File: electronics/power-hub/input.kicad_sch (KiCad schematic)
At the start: 12 parts, among them J1 24V IN, Q1 SUD50P06-15

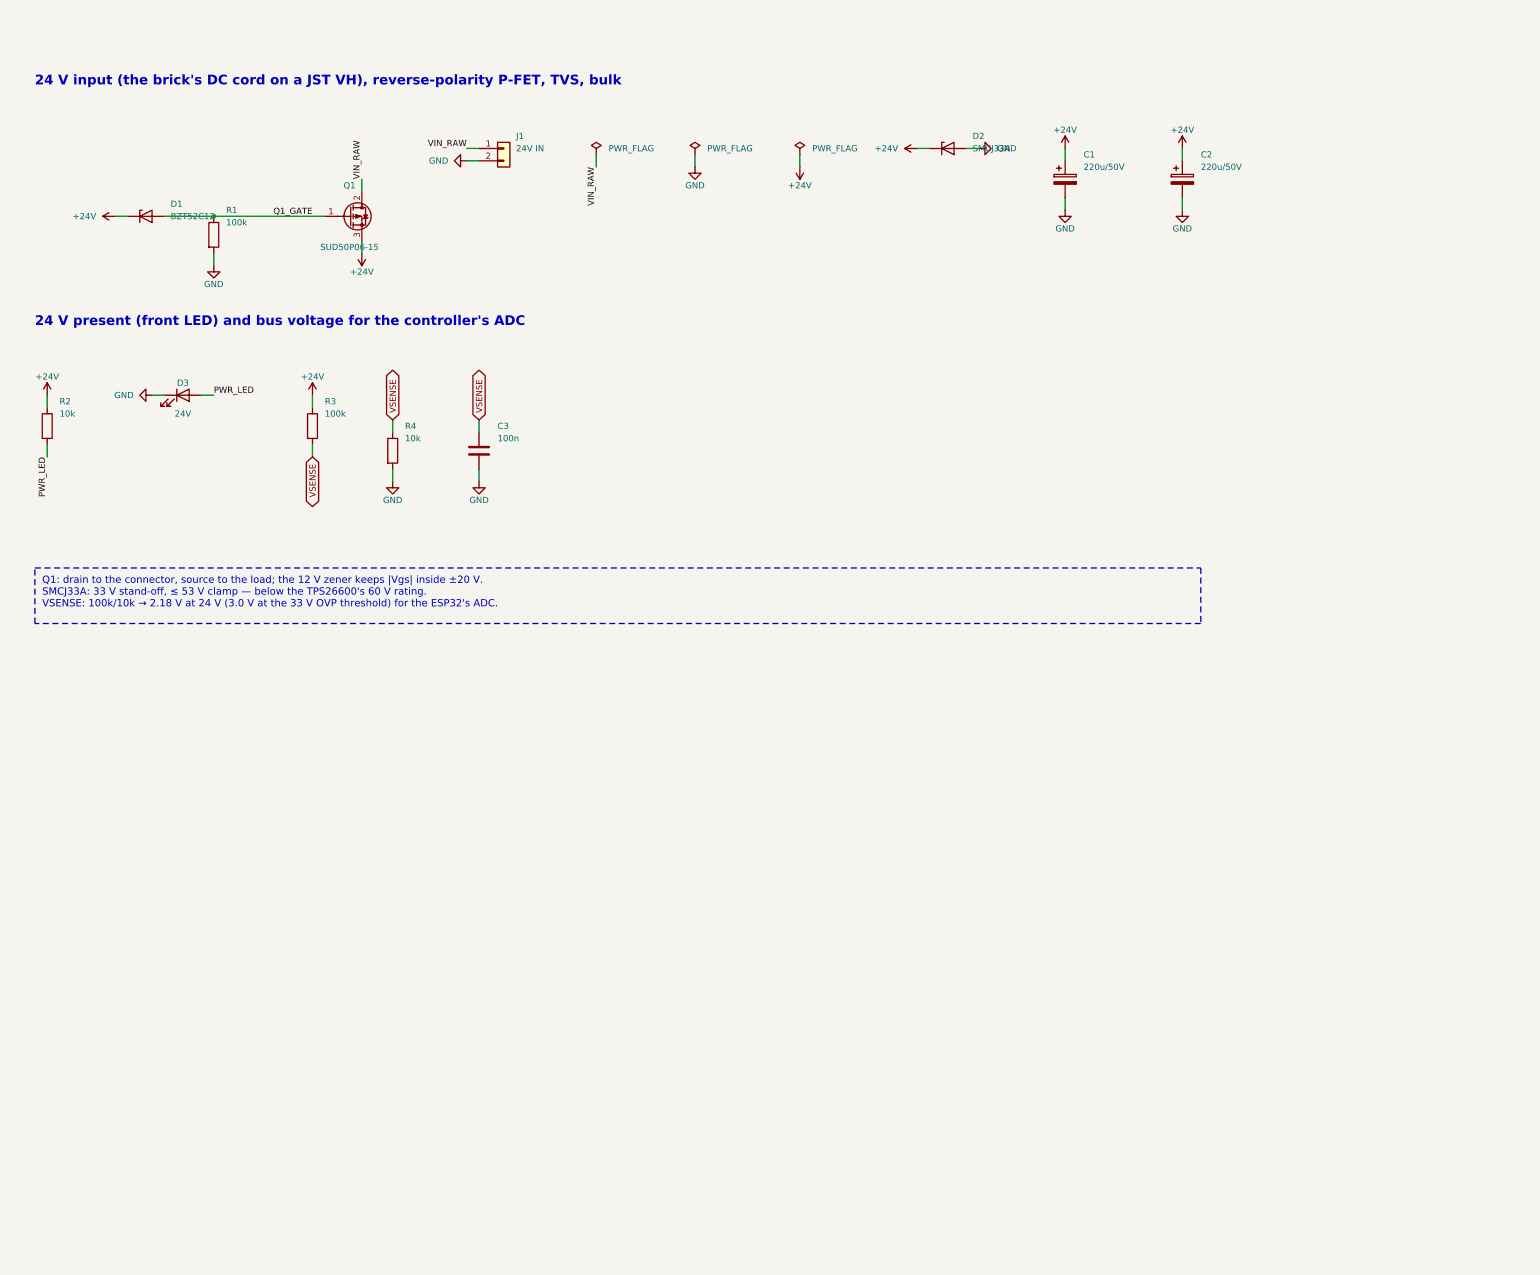
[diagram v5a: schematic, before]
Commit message: Power hub v0.5: USB-C PD input (AP33772S), 4 layers, rows off until enabled
The rack now runs from one USB PD 3.1 charger instead of the GST60A24 brick.

Hub v0.5 (76 x 140 mm, 4 layers, In1 GND, In2 VRACK/+3V3):
* AP33772S sink: 20 V at power-up (VSEL 39k), 28 V EPR on the controller's
  request, never 36/48 V; 5 mOhm Kelvin shunt, back-to-back IRF7842 switch,
  SMAJ30A TVS, NTC by the switch, interrupt and I2C to the ESP32-S3.
* USB4105 5 A receptacle; the controller's buck runs from VBUS (5-28 V),
  ahead of the switch.
* Every row's TPS26600 is off until the controller drives ROW_EN (SHDN pulled
  low); IMON per row; front PD LED.
* ERC 0, DRC 0 errors, 0 unconnected, parity 0; 146 3D models, 0 stand-ins.

Power box: 84 x 148 x 35 mm, hub only (no brick, no cradles), rear USB-C
cut-out, lid on corner lugs.  Viewer, BOM (charger + 5 A e-marked cable,
4-layer JLC estimate) and docs (power, mechanical, cabling, assembly,
electronics) follow.

Co-Authored-By: Claude Opus 5.5 <noreply@anthropic.com>
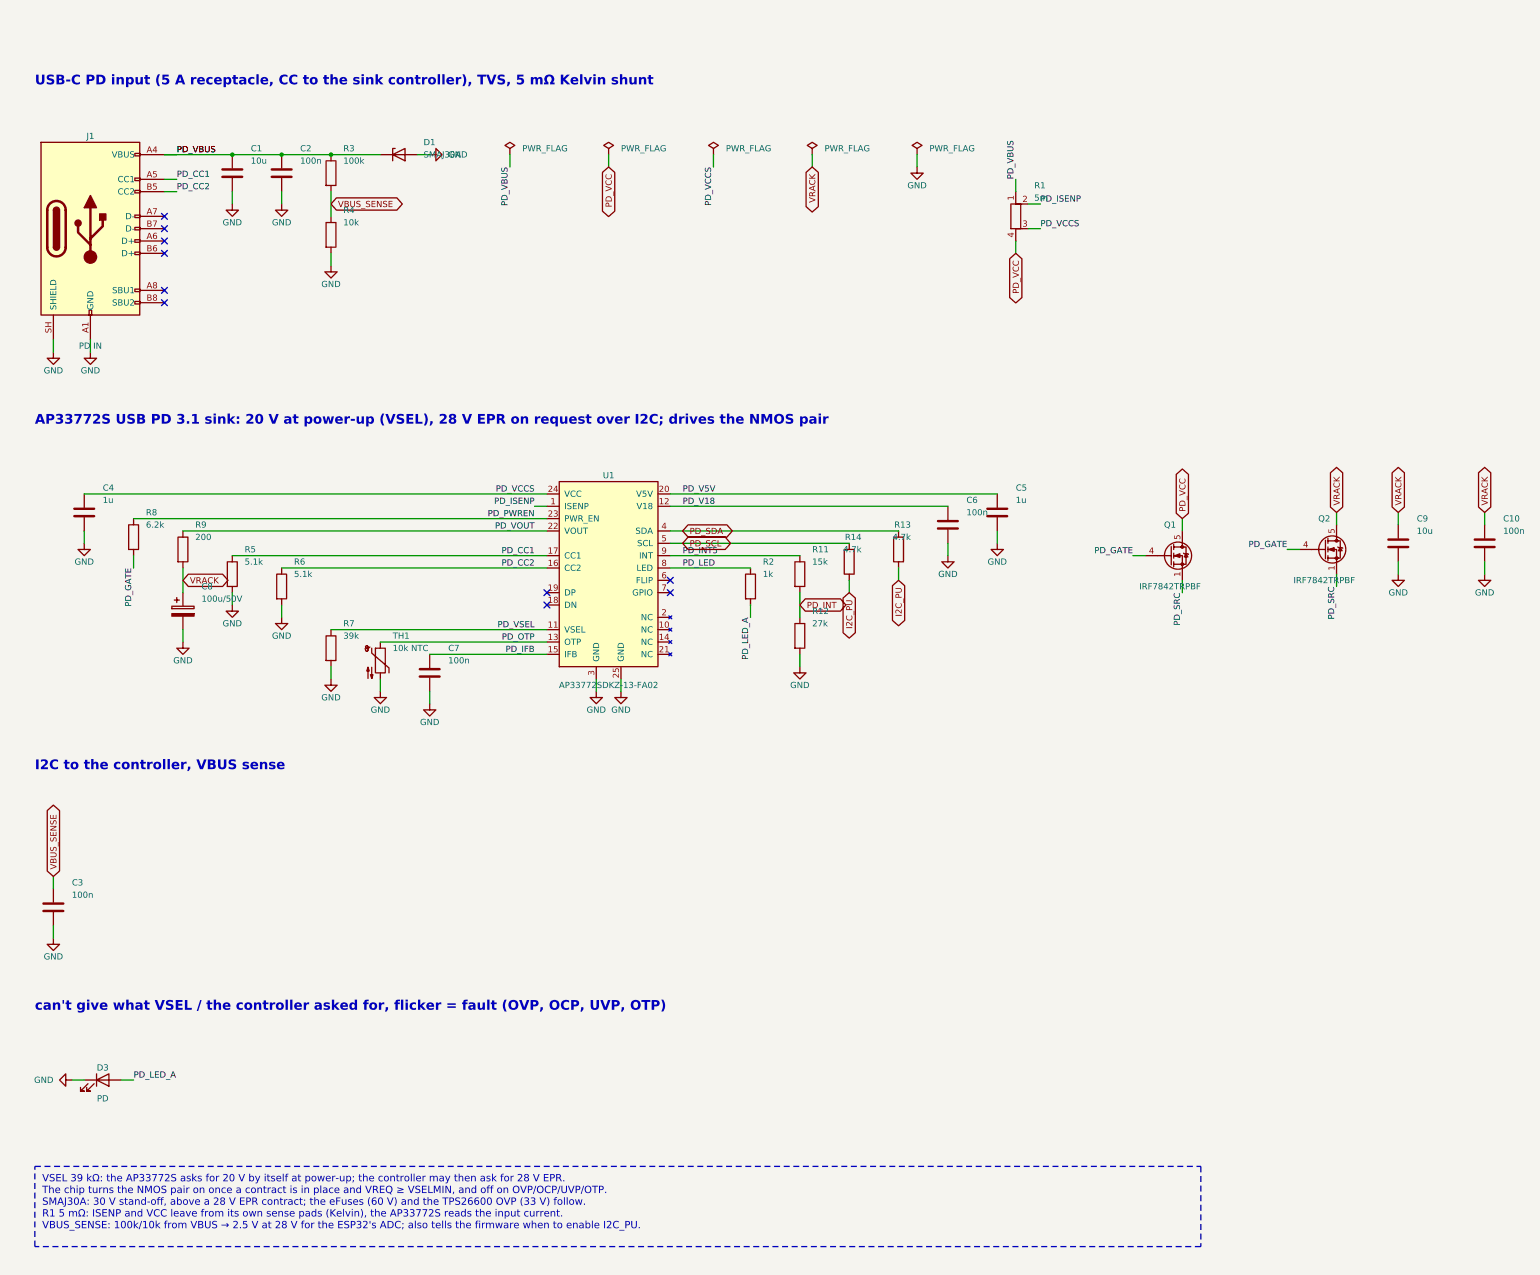
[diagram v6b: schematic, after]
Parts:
- removed D2: SMCJ33A, Diode_SMD:D_SMC, symbol Device:D_Zener
- added C10, C6, C7: 100n, Capacitor_SMD:C_0603_1608Metric, symbol Device:C
- added C4, C5: 1u, Capacitor_SMD:C_0603_1608Metric, symbol Device:C
- added C8: 100u/50V, Capacitor_SMD:CP_Elec_8x10, symbol Device:C_Polarized
- added C9: 10u, Capacitor_SMD:C_1206_3216Metric, symbol Device:C
- added Q2: IRF7842TRPBF, Package_SO:SOIC-8_3.9x4.9mm_P1.27mm, symbol Transistor_FET:Si4162DY
- added R11: 15k, Resistor_SMD:R_0603_1608Metric, symbol Device:R
- added R12: 27k, Resistor_SMD:R_0603_1608Metric, symbol Device:R
- added R13, R14: 4.7k, Resistor_SMD:R_0603_1608Metric, symbol Device:R
- added R5, R6: 5.1k, Resistor_SMD:R_0603_1608Metric, symbol Device:R
- added R7: 39k, Resistor_SMD:R_0603_1608Metric, symbol Device:R
- added R8: 6.2k, Resistor_SMD:R_0603_1608Metric, symbol Device:R
- added R9: 200, Resistor_SMD:R_0603_1608Metric, symbol Device:R
- added TH1: 10k NTC, Resistor_SMD:R_0603_1608Metric, symbol Device:Thermistor_NTC
- added U1: AP33772SDKZ-13-FA02, Package_DFN_QFN:QFN-24-1EP_4x4mm_P0.5mm_EP2.7x2.7mm, symbol bench:AP33772S
- C1: value 220u/50V -> 10u; footprint Capacitor_SMD:CP_Elec_10x10 -> Capacitor_SMD:C_1206_3216Metric; symbol Device:C_Polarized -> Device:C; LCSC C3358 -> C13585; MPN RVT1H221M1010 -> CL31A106KBHNNNE; Manufacturer Honor Elec -> Samsung Electro-Mechanics
- C2: value 220u/50V -> 100n; footprint Capacitor_SMD:CP_Elec_10x10 -> Capacitor_SMD:C_0603_1608Metric; symbol Device:C_Polarized -> Device:C; LCSC C3358 -> C14663; MPN RVT1H221M1010 -> CC0603KRX7R9BB104; Manufacturer Honor Elec -> YAGEO
- D1: value BZT52C12 -> SMAJ30A; footprint Diode_SMD:D_SOD-123 -> Diode_SMD:D_SMA; LCSC C43491 -> C113965; MPN BZT52C12 -> SMAJ30A; Manufacturer CJ -> MDD
- D3: value 24V -> PD
- J1: value 24V IN -> PD IN; footprint Connector_JST:JST_VH_S2P-VH_1x02_P3.96mm_Horizontal -> Connector_USB:USB_C_Receptacle_GCT_USB4105-xx-A_16P_TopMnt_Horizontal; symbol Connector_Generic:Conn_01x02 -> Connector:USB_C_Receptacle_USB2.0_16P; LCSC C160355 -> C5184243; MPN S2P-VH(LF)(SN) -> USB4105-GF-A-120; Manufacturer JST -> GCT
- Q1: value SUD50P06-15 -> IRF7842TRPBF; footprint Package_TO_SOT_SMD:TO-252-2 -> Package_SO:SOIC-8_3.9x4.9mm_P1.27mm; symbol Transistor_FET:SUD50P06-15 -> Transistor_FET:Si4162DY; Alternative C7472883 (TECH PUBLIC), C141584 (Vishay) -> (none); LCSC C7503186 -> C495809; MPN SUD50P06-15 -> IRF7842TRPBF; Manufacturer UMW / Vishay -> Infineon
- R1: value 100k -> 5m; footprint Resistor_SMD:R_0603_1608Metric -> bench:R_1206_3216Metric_Kelvin; symbol Device:R -> Device:R_Shunt; LCSC C25803 -> C2988648; MPN 0603WAF1003T5E -> HoLLR1206-1W-5mR-1%; Manufacturer UNI-ROYAL(Uniroyal Elec) -> Milliohm
- R2: value 10k -> 1k; footprint Resistor_SMD:R_0805_2012Metric -> Resistor_SMD:R_0603_1608Metric; LCSC C17414 -> C21190; MPN 0805W8F1002T5E -> 0603WAF1001T5E
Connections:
- net GND: now also D1.2 (A), J1.A1 (GND), J1.A12 (GND), J1.B1 (GND), J1.B12 (GND), J1.SH (SHIELD), C10.2, C4.2, C5.2, C6.2, C7.2, C8.2, C9.2, R12.2, R5.2, R6.2, R7.2, TH1.2, U1.25 (GND), U1.3 (GND); no longer J1.2 (Pin_2), R1.2
- net +24V renamed PD_VBUS
- net PD_VBUS: now also J1.A4 (VBUS), J1.A9 (VBUS), J1.B4 (VBUS), J1.B9 (VBUS), R1.1; no longer Q1.3 (S), R2.1
- net PWR_LED renamed PD_LED_A
- removed net Q1_GATE: D1.2 (A), Q1.1 (G), R1.1
- net VIN_RAW renamed PD_SRC
- net PD_SRC: now also Q1.1 (S), Q1.3 (S), Q2.1 (S), Q2.2 (S), Q2.3 (S); no longer J1.1 (Pin_1)
- net VSENSE renamed VBUS_SENSE
- new net I2C_PU: R13.1, R14.1
- new net PD_CC1: J1.A5 (CC1), R5.1, U1.17 (CC1)
- new net PD_CC2: J1.B5 (CC2), R6.1, U1.16 (CC2)
- new net PD_GATE: Q1.4 (G), Q2.4 (G), R8.2
- new net PD_IFB: C7.1, U1.15 (IFB)
- new net PD_INT: R11.2, R12.1
- new net PD_INT5: R11.1, U1.9 (INT)
- new net PD_ISENP: R1.2, U1.1 (ISENP)
- new net PD_LED: R2.1, U1.8 (LED)
- new net PD_OTP: TH1.1, U1.13 (OTP)
- new net PD_PWREN: R8.1, U1.23 (PWR_EN)
- new net PD_SCL: R14.2, U1.5 (SCL)
- new net PD_SDA: R13.2, U1.4 (SDA)
- new net PD_V18: C6.1, U1.12 (V18)
- new net PD_V5V: C5.1, U1.20 (V5V)
- new net PD_VCC: Q1.5 (D), Q1.6 (D), Q1.7 (D), Q1.8 (D), R1.4
- new net PD_VCCS: C4.1, R1.3, U1.24 (VCC)
- new net PD_VOUT: R9.1, U1.22 (VOUT)
- new net PD_VSEL: R7.1, U1.11 (VSEL)
- new net VRACK: C10.1, C8.1, C9.1, Q2.5 (D), Q2.6 (D), Q2.7 (D), Q2.8 (D), R9.2
- no-connect marks 0 -> 10
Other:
- note added: "AP33772S USB PD 3.1 sink: 20 V at power-up (VSEL), 28 V EPR on request over I2C; drives the NMOS pair"
- note added: "I2C to the controller, VBUS sense"
- note added: "USB-C PD input (5 A receptacle, CC to the sink controller), TVS, 5 mΩ Kelvin shunt"
- note added: "can't give what VSEL / the controller asked for, flicker = fault (OVP, OCP, UVP, OTP)"
- note removed: "24 V input (the brick's DC cord on a JST VH), reverse-polarity P-FET, TVS, bulk"
- note removed: "24 V present (front LED) and bus voltage for the controller's ADC"
- title: Power hub — 24 V input and protection -> Power hub — USB-C PD input
- moved on the sheet: C3, D1, D3, Q1, R2, R3, R4

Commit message: Power hub: U1 is the AP33772S FA01 (5 V first), bought through JLC Global Sourcing
The FA02 (VSEL: 20 V by itself) is out of stock everywhere until
≈ 14/12/2026; the user approved the FA01 (2026-10-19): same die, package,
pinout and I2C map, pins 7 and 11 NC.  It takes the charger's 5 V first;
the firmware (7b8a705) sets VSELMIN to 15 V and asks for 20 V / 28 V EPR,
and the rows stay locked out below 15 V.  R7 (an FA02's VSEL resistor)
stays fitted, so an FA02 drops in later.

- catalog: AP33772SDKZ-13-FA01, LCSC C24374260 (0 stock), DigiKey via
  JLC Global Sourcing.
- Hub schematic notes and BOMs regenerated; the routing is the same
  session re-imported (1241 segments, 583 vias, as on main).  ERC 0,
  DRC 0 errors / 0 unconnected / parity 0 (one silk warning, as on main).
- bom.py hub estimate ≈ $227: + $13.30 for 5 parts through Global
  Sourcing (JLC's markup reported ≈ 50 %, no official figure) and
  ≈ 2 weeks for them to reach JLC.
- docs/power.md step 1 and sourcing, electronics.md hub rows,
  bom/sourcing.md: the choice.

Co-Authored-By: Claude Opus 5.5 <noreply@anthropic.com>
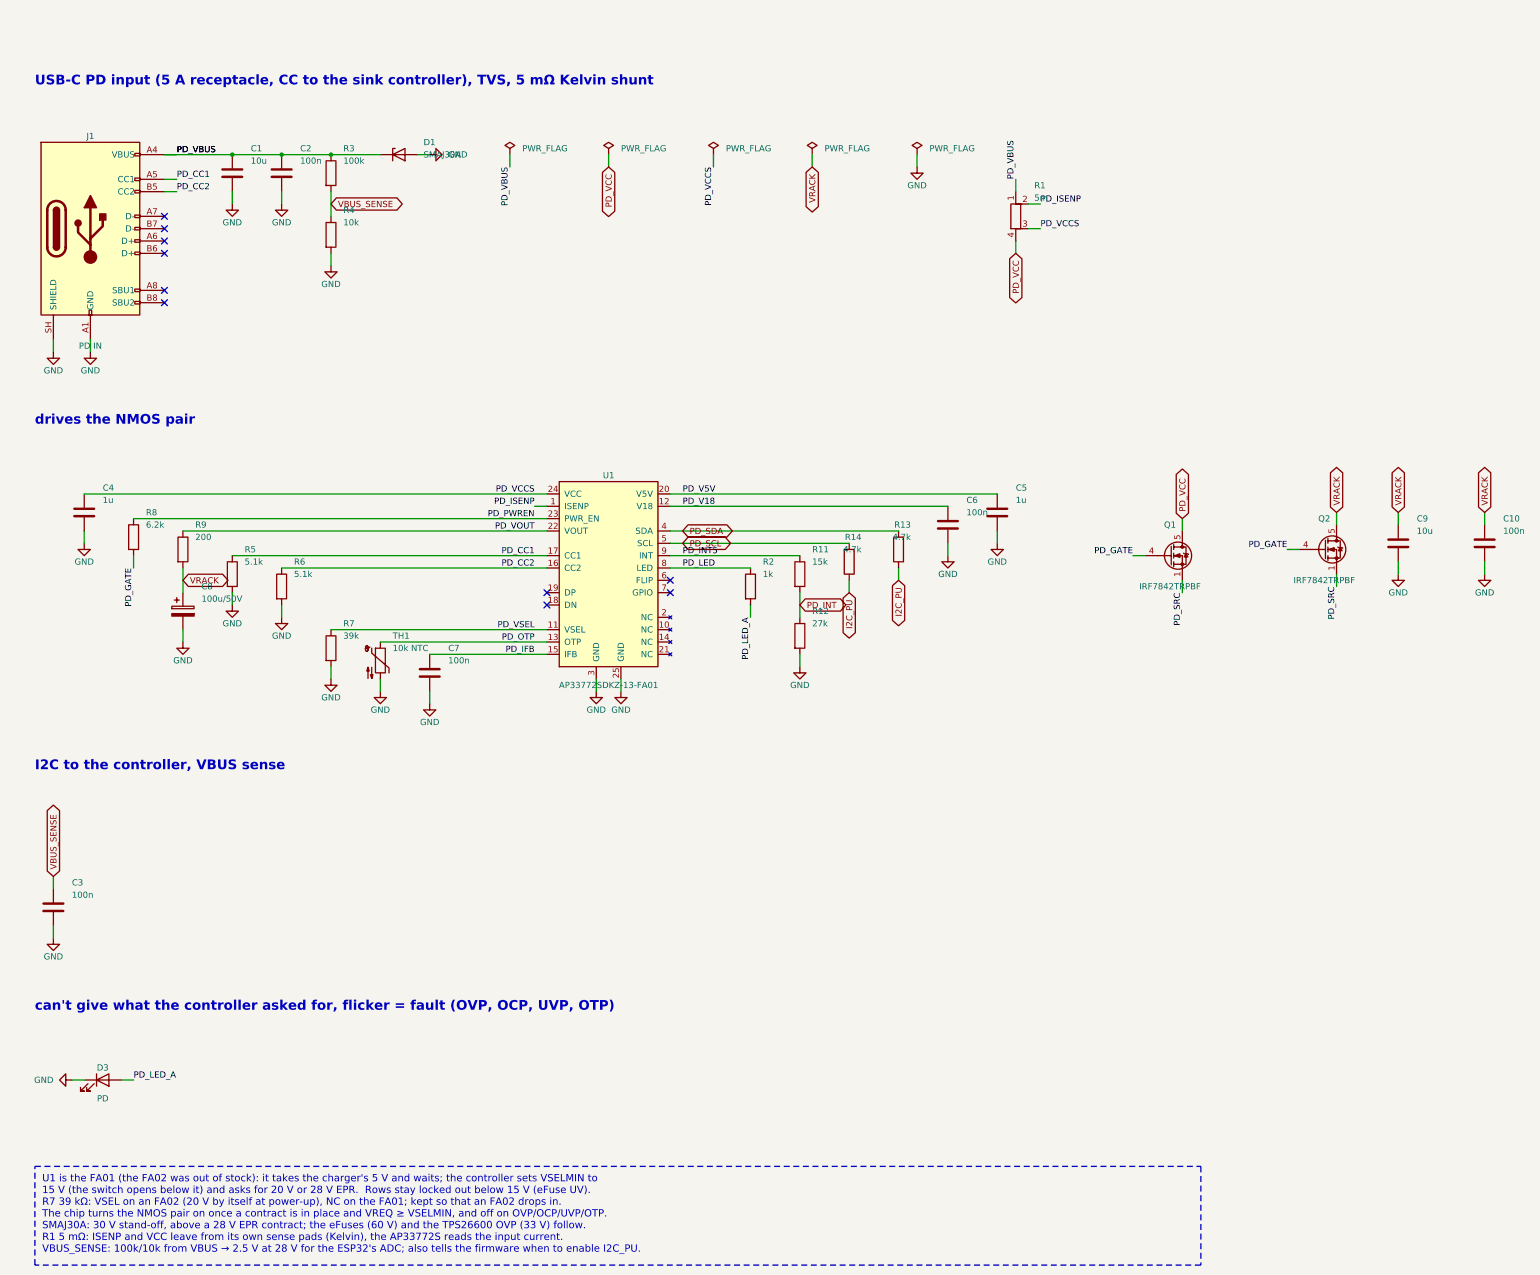
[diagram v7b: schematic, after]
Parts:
- U1: value AP33772SDKZ-13-FA02 -> AP33772SDKZ-13-FA01; Alternative LCSC stock was 0 on 2026-10-18: JLC global sourcing (DigiKe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 -> LCSC/JLC stock 0 on 2026-10-19: JLC Global Sourcing from Di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; LCSC C50341643 -> C24374260; MPN AP33772SDKZ-13-FA02 -> AP33772SDKZ-13-FA01
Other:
- note added: "can't give what the controller asked for, flicker = fault (OVP, OCP, UVP, OTP)"
- note added: "drives the NMOS pair"
- note removed: "AP33772S USB PD 3.1 sink: 20 V at power-up (VSEL), 28 V EPR on request over I2C; drives the NMOS pair"
- note removed: "can't give what VSEL / the controller asked for, flicker = fault (OVP, OCP, UVP, OTP)"
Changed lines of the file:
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@@
 		)
 	)
-	(text "AP33772S USB PD 3.1 sink: 20 V at power-up (VSEL), 28 V EPR on request over I2C; drives the NMOS pair"
+	(text "drives the NMOS pair"
 		(exclude_from_sim no)
 		(at 20.32 100.33 0)
@@
 		)
 	)
-	(text "can't give what VSEL / the controller asked for, flicker = fault (OVP, OCP, UVP, OTP)"
+	(text "can't give what the controller asked for, flicker = fault (OVP, OCP, UVP, OTP)"
 		(exclude_from_sim no)
 		(at 20.32 220.98 0)
@@
 			)
 		)
-		(property "Value" "AP33772SDKZ-13-FA02"
+		(property "Value" "AP33772SDKZ-13-FA01"
 			(at 138.43 153.67 0)
 			(effects
@@
 			)
 		)
-		(property "MPN" "AP33772SDKZ-13-FA02"
+		(property "MPN" "AP33772SDKZ-13-FA01"
 			(at 138.43 129.54 0)
 			(effects
@@
 			)
 		)
-		(property "LCSC" "C50341643"
+		(property "LCSC" "C24374260"
 			(at 138.43 129.54 0)
 			(effects
@@
 			)
 		)
-		(property "Alternative" "LCSC stock was 0 on 2026-10-18: JLC global sourcing (DigiKey/Mouser) or a consigned reel"
+		(property "Alternative" "LCSC/JLC stock 0 on 2026-10-19: JLC Global Sourcing from DigiKey (365 in stock, €2.09 @1, €1.54 @10); the FA02 drops in from ≈ 14/12/2026"
 			(at 138.43 129.54 0)
 			(effects
@@
 		)
 	)
-	(text_box "VSEL 39 kΩ: the AP33772S asks for 20 V by itself at power-up; the controller may then ask for 28 V EPR.\nThe chip turns the NMOS pair on once a contract is in place and VREQ ≥ VSELMIN, and off on OVP/OCP/UVP/OTP.\nSMAJ30A: 30 V stand-off, above a 28 V EPR contract; the eFuses (60 V) and the TPS26600 OVP (33 V) follow.\nR1 5 mΩ: ISENP and VCC leave from its own sense pads (Kelvin), the AP33772S reads the input current.\nVBUS_SENSE: 100k/10k from VBUS → 2.5 V at 28 V for the ESP32's ADC; also tells the firmware when to enable I2C_PU."
+	(text_box "U1 is the FA01 (the FA02 was out of stock): it takes the charger's 5 V and waits; the controller sets VSELMIN to\n  15 V (the switch opens below it) and asks for 20 V or 28 V EPR.  Rows stay locked out below 15 V (eFuse UV).\nR7 39 kΩ: VSEL on an FA02 (20 V by itself at power-up), NC on the FA01; kept so that an FA02 drops in.\nThe chip turns the NMOS pair on once a contract is in place and VREQ ≥ VSELMIN, and off on OVP/OCP/UVP/OTP.\nSMAJ30A: 30 V stand-off, above a 28 V EPR contract; the eFuses (60 V) and the TPS26600 OVP (33 V) follow.\nR1 5 mΩ: ISENP and VCC leave from its own sense pads (Kelvin), the AP33772S reads the input current.\nVBUS_SENSE: 100k/10k from VBUS → 2.5 V at 28 V for the ESP32's ADC; also tells the firmware when to enable I2C_PU."
 		(exclude_from_sim no)
 		(at 20.32 252.73 0)
-		(size 240.03 16.51)
+		(size 240.03 20.32)
 		(margins 1.5 1.5 1.5 1.5)
 		(stroke
